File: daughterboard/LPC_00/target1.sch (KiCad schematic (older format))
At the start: 8 parts, among them U1 LPC1114FDH28_102_5

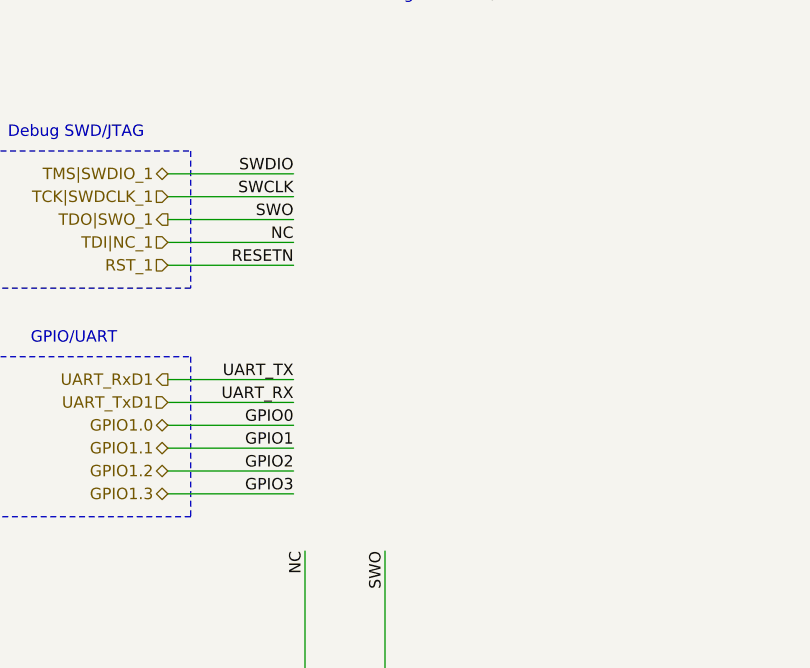
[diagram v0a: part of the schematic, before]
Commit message: added testpoints to daughterboards, updated readme
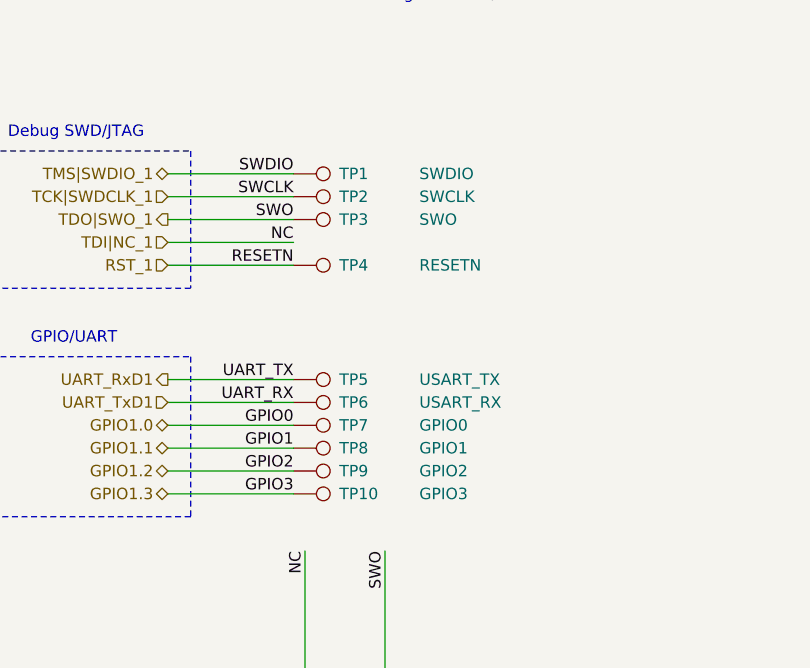
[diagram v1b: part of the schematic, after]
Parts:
- added TP1: SWDIO, symbol Connector:TestPoint
- added TP10: GPIO3, symbol Connector:TestPoint
- added TP2: SWCLK, symbol Connector:TestPoint
- added TP3: SWO, symbol Connector:TestPoint
- added TP4: RESETN, symbol Connector:TestPoint
- added TP5: USART_TX, symbol Connector:TestPoint
- added TP6: USART_RX, symbol Connector:TestPoint
- added TP7: GPIO0, symbol Connector:TestPoint
- added TP8: GPIO1, symbol Connector:TestPoint
- added TP9: GPIO2, symbol Connector:TestPoint
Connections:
- net GPIO1.0: now also TP7.1
- net GPIO1.1: now also TP8.1
- net GPIO1.2: now also TP9.1
- net GPIO1.3: now also TP10.1
- net RST_1: now also TP4.1
- net TCK|SWDCLK_1: now also TP2.1
- net TDO|SWO_1: now also TP3.1
- net TMS|SWDIO_1: now also TP1.1
- net UART_RxD1: now also TP5.1
- net UART_TxD1: now also TP6.1
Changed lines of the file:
@@
 NoConn ~ 5200 3650
 NoConn ~ 5200 3850
+$Comp
+L Connector:TestPoint TP?
+U 1 1 6191DBB6
+P 2150 1700
+AR Path="/616688D6/6191DBB6" Ref="TP?"  Part="1"
+AR Path="/61667F91/6191DBB6" Ref="TP1"  Part="1"
+F 0 "TP1" V 2150 1900 50  0000 L CNN
+F 1 "SWDIO" V 2150 2250 50  0000 L CNN
+F 2 "" H 2350 1700 50  0001 C CNN
+F 3 "~" H 2350 1700 50  0001 C CNN
+	1    2150 1700
+	0    1    1    0
+$EndComp
+$Comp
+L Connector:TestPoint TP?
+U 1 1 6191DBBC
+P 2150 1800
+AR Path="/616688D6/6191DBBC" Ref="TP?"  Part="1"
+AR Path="/61667F91/6191DBBC" Ref="TP2"  Part="1"
+F 0 "TP2" V 2150 2000 50  0000 L CNN
+F 1 "SWCLK" V 2150 2350 50  0000 L CNN
+F 2 "" H 2350 1800 50  0001 C CNN
+F 3 "~" H 2350 1800 50  0001 C CNN
+	1    2150 1800
+	0    1    1    0
+$EndComp
+$Comp
+L Connector:TestPoint TP?
+U 1 1 6191DBC2
+P 2150 1900
+AR Path="/616688D6/6191DBC2" Ref="TP?"  Part="1"
+AR Path="/61667F91/6191DBC2" Ref="TP3"  Part="1"
+F 0 "TP3" V 2150 2100 50  0000 L CNN
+F 1 "SWO" V 2150 2450 50  0000 L CNN
+F 2 "" H 2350 1900 50  0001 C CNN
+F 3 "~" H 2350 1900 50  0001 C CNN
+	1    2150 1900
+	0    1    1    0
+$EndComp
+$Comp
+L Connector:TestPoint TP?
+U 1 1 6191DBC8
+P 2150 2100
+AR Path="/616688D6/6191DBC8" Ref="TP?"  Part="1"
+AR Path="/61667F91/6191DBC8" Ref="TP4"  Part="1"
+F 0 "TP4" V 2150 2300 50  0000 L CNN
+F 1 "RESETN" V 2150 2650 50  0000 L CNN
+F 2 "" H 2350 2100 50  0001 C CNN
+F 3 "~" H 2350 2100 50  0001 C CNN
+	1    2150 2100
+	0    1    1    0
+$EndComp
+$Comp
+L Connector:TestPoint TP?
+U 1 1 6191DBCE
+P 2150 2600
+AR Path="/616688D6/6191DBCE" Ref="TP?"  Part="1"
+AR Path="/61667F91/6191DBCE" Ref="TP5"  Part="1"
+F 0 "TP5" V 2150 2800 50  0000 L CNN
+F 1 "USART_TX" V 2150 3150 50  0000 L CNN
+F 2 "" H 2350 2600 50  0001 C CNN
+F 3 "~" H 2350 2600 50  0001 C CNN
+	1    2150 2600
+	0    1    1    0
+$EndComp
+$Comp
+L Connector:TestPoint TP?
+U 1 1 6191DBD4
+P 2150 2700
+AR Path="/616688D6/6191DBD4" Ref="TP?"  Part="1"
+AR Path="/61667F91/6191DBD4" Ref="TP6"  Part="1"
+F 0 "TP6" V 2150 2900 50  0000 L CNN
+F 1 "USART_RX" V 2150 3250 50  0000 L CNN
+F 2 "" H 2350 2700 50  0001 C CNN
+F 3 "~" H 2350 2700 50  0001 C CNN
+	1    2150 2700
+	0    1    1    0
+$EndComp
+$Comp
+L Connector:TestPoint TP?
+U 1 1 6191DBDA
+P 2150 2800
+AR Path="/616688D6/6191DBDA" Ref="TP?"  Part="1"
+AR Path="/61667F91/6191DBDA" Ref="TP7"  Part="1"
+F 0 "TP7" V 2150 3000 50  0000 L CNN
+F 1 "GPIO0" V 2150 3350 50  0000 L CNN
+F 2 "" H 2350 2800 50  0001 C CNN
+F 3 "~" H 2350 2800 50  0001 C CNN
+	1    2150 2800
+	0    1    1    0
+$EndComp
+$Comp
+L Connector:TestPoint TP?
+U 1 1 6191DBE0
+P 2150 2900
+AR Path="/616688D6/6191DBE0" Ref="TP?"  Part="1"
+AR Path="/61667F91/6191DBE0" Ref="TP8"  Part="1"
+F 0 "TP8" V 2150 3100 50  0000 L CNN
+F 1 "GPIO1" V 2150 3450 50  0000 L CNN
+F 2 "" H 2350 2900 50  0001 C CNN
+F 3 "~" H 2350 2900 50  0001 C CNN
+	1    2150 2900
+	0    1    1    0
+$EndComp
+$Comp
+L Connector:TestPoint TP?
+U 1 1 6191DBE6
+P 2150 3000
+AR Path="/616688D6/6191DBE6" Ref="TP?"  Part="1"
+AR Path="/61667F91/6191DBE6" Ref="TP9"  Part="1"
+F 0 "TP9" V 2150 3200 50  0000 L CNN
+F 1 "GPIO2" V 2150 3550 50  0000 L CNN
+F 2 "" H 2350 3000 50  0001 C CNN
+F 3 "~" H 2350 3000 50  0001 C CNN
+	1    2150 3000
+	0    1    1    0
+$EndComp
+$Comp
+L Connector:TestPoint TP?
+U 1 1 6191DBEC
+P 2150 3100
+AR Path="/616688D6/6191DBEC" Ref="TP?"  Part="1"
+AR Path="/61667F91/6191DBEC" Ref="TP10"  Part="1"
+F 0 "TP10" V 2150 3300 50  0000 L CNN
+F 1 "GPIO3" V 2150 3650 50  0000 L CNN
+F 2 "" H 2350 3100 50  0001 C CNN
+F 3 "~" H 2350 3100 50  0001 C CNN
+	1    2150 3100
+	0    1    1    0
+$EndComp
 $EndSCHEMATC

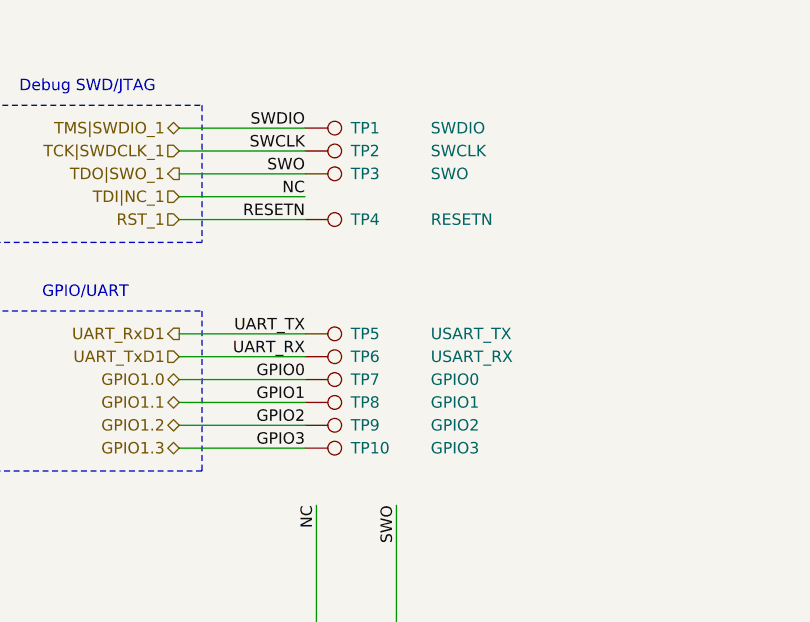
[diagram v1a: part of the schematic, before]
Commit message: sarted with LPC daughterboard layout
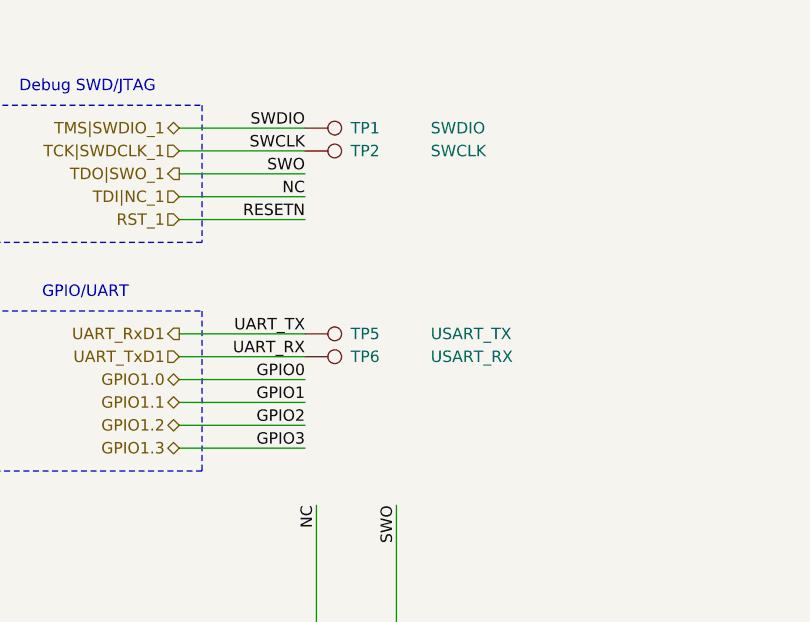
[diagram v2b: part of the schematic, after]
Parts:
- removed TP10: GPIO3, symbol Connector:TestPoint
- removed TP3: SWO, symbol Connector:TestPoint
- removed TP4: RESETN, symbol Connector:TestPoint
- removed TP7: GPIO0, symbol Connector:TestPoint
- removed TP8: GPIO1, symbol Connector:TestPoint
- removed TP9: GPIO2, symbol Connector:TestPoint
- C1, C2, C3: footprint (none) -> Capacitor_SMD:C_0603_1608Metric_Pad1.05x0.95mm_HandSolder
- JP1: footprint (none) -> Jumper:SolderJumper-2_P1.3mm_Open_TrianglePad1.0x1.5mm
- R1, R2, R3: footprint (none) -> Resistor_SMD:R_0603_1608Metric_Pad1.05x0.95mm_HandSolder
- TP1, TP2, TP5, TP6: footprint (none) -> TestPoint:TestPoint_Pad_1.0x1.0mm
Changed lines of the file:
@@
 F 0 "R2" H 2259 4346 50  0000 L CNN
 F 1 "100k" H 2259 4255 50  0000 L CNN
-F 2 "" H 2200 4300 50  0001 C CNN
+F 2 "Resistor_SMD:R_0603_1608Metric_Pad1.05x0.95mm_HandSolder" H 2200 4300 50  0001 C CNN
 F 3 "~" H 2200 4300 50  0001 C CNN
 	1    2200 4300
@@
 F 0 "R1" H 859 4346 50  0000 L CNN
 F 1 "100k" H 859 4255 50  0000 L CNN
-F 2 "" H 800 4300 50  0001 C CNN
+F 2 "Resistor_SMD:R_0603_1608Metric_Pad1.05x0.95mm_HandSolder" H 800 4300 50  0001 C CNN
 F 3 "~" H 800 4300 50  0001 C CNN
 	1    800  4300
@@
 F 0 "JP1" V 1404 4368 50  0000 L CNN
 F 1 "NRST" V 1495 4368 50  0000 L CNN
-F 2 "" H 1450 4300 50  0001 C CNN
+F 2 "Jumper:SolderJumper-2_P1.3mm_Open_TrianglePad1.0x1.5mm" H 1450 4300 50  0001 C CNN
 F 3 "~" H 1450 4300 50  0001 C CNN
 	1    1450 4300
@@
 F 0 "R3" H 2609 4346 50  0000 L CNN
 F 1 "100k" H 2609 4255 50  0000 L CNN
-F 2 "" H 2550 4300 50  0001 C CNN
+F 2 "Resistor_SMD:R_0603_1608Metric_Pad1.05x0.95mm_HandSolder" H 2550 4300 50  0001 C CNN
 F 3 "~" H 2550 4300 50  0001 C CNN
 	1    2550 4300
@@
 F 0 "C2" H 7892 2046 50  0000 L CNN
 F 1 "100n" H 7892 1955 50  0000 L CNN
-F 2 "" H 7800 2000 50  0001 C CNN
+F 2 "Capacitor_SMD:C_0603_1608Metric_Pad1.05x0.95mm_HandSolder" H 7800 2000 50  0001 C CNN
 F 3 "~" H 7800 2000 50  0001 C CNN
 	1    7800 2000
@@
 F 0 "C3" H 8292 2046 50  0000 L CNN
 F 1 "100n" H 8292 1955 50  0000 L CNN
-F 2 "" H 8200 2000 50  0001 C CNN
+F 2 "Capacitor_SMD:C_0603_1608Metric_Pad1.05x0.95mm_HandSolder" H 8200 2000 50  0001 C CNN
 F 3 "~" H 8200 2000 50  0001 C CNN
 	1    8200 2000
@@
 F 0 "C1" H 7392 2046 50  0000 L CNN
 F 1 "4.7u" H 7392 1955 50  0000 L CNN
-F 2 "" H 7300 2000 50  0001 C CNN
+F 2 "Capacitor_SMD:C_0603_1608Metric_Pad1.05x0.95mm_HandSolder" H 7300 2000 50  0001 C CNN
 F 3 "~" H 7300 2000 50  0001 C CNN
 	1    7300 2000
@@
 F 0 "TP1" V 2150 1900 50  0000 L CNN
 F 1 "SWDIO" V 2150 2250 50  0000 L CNN
-F 2 "" H 2350 1700 50  0001 C CNN
+F 2 "TestPoint:TestPoint_Pad_1.0x1.0mm" H 2350 1700 50  0001 C CNN
 F 3 "~" H 2350 1700 50  0001 C CNN
 	1    2150 1700
@@
 F 0 "TP2" V 2150 2000 50  0000 L CNN
 F 1 "SWCLK" V 2150 2350 50  0000 L CNN
-F 2 "" H 2350 1800 50  0001 C CNN
+F 2 "TestPoint:TestPoint_Pad_1.0x1.0mm" H 2350 1800 50  0001 C CNN
 F 3 "~" H 2350 1800 50  0001 C CNN
 	1    2150 1800
-	0    1    1    0
-$EndComp
-$Comp
-L Connector:TestPoint TP?
-U 1 1 6191DBC2
-P 2150 1900
-AR Path="/616688D6/6191DBC2" Ref="TP?"  Part="1"
-AR Path="/61667F91/6191DBC2" Ref="TP3"  Part="1"
-F 0 "TP3" V 2150 2100 50  0000 L CNN
-F 1 "SWO" V 2150 2450 50  0000 L CNN
-F 2 "" H 2350 1900 50  0001 C CNN
-F 3 "~" H 2350 1900 50  0001 C CNN
-	1    2150 1900
-	0    1    1    0
-$EndComp
-$Comp
-L Connector:TestPoint TP?
-U 1 1 6191DBC8
-P 2150 2100
-AR Path="/616688D6/6191DBC8" Ref="TP?"  Part="1"
-AR Path="/61667F91/6191DBC8" Ref="TP4"  Part="1"
-F 0 "TP4" V 2150 2300 50  0000 L CNN
-F 1 "RESETN" V 2150 2650 50  0000 L CNN
-F 2 "" H 2350 2100 50  0001 C CNN
-F 3 "~" H 2350 2100 50  0001 C CNN
-	1    2150 2100
 	0    1    1    0
 $EndComp
@@
 F 0 "TP5" V 2150 2800 50  0000 L CNN
 F 1 "USART_TX" V 2150 3150 50  0000 L CNN
-F 2 "" H 2350 2600 50  0001 C CNN
+F 2 "TestPoint:TestPoint_Pad_1.0x1.0mm" H 2350 2600 50  0001 C CNN
 F 3 "~" H 2350 2600 50  0001 C CNN
 	1    2150 2600
@@
 F 0 "TP6" V 2150 2900 50  0000 L CNN
 F 1 "USART_RX" V 2150 3250 50  0000 L CNN
-F 2 "" H 2350 2700 50  0001 C CNN
+F 2 "TestPoint:TestPoint_Pad_1.0x1.0mm" H 2350 2700 50  0001 C CNN
 F 3 "~" H 2350 2700 50  0001 C CNN
 	1    2150 2700
 	0    1    1    0
 $EndComp
-$Comp
-L Connector:TestPoint TP?
-U 1 1 6191DBDA
-P 2150 2800
-AR Path="/616688D6/6191DBDA" Ref="TP?"  Part="1"
-AR Path="/61667F91/6191DBDA" Ref="TP7"  Part="1"
-F 0 "TP7" V 2150 3000 50  0000 L CNN
-F 1 "GPIO0" V 2150 3350 50  0000 L CNN
-F 2 "" H 2350 2800 50  0001 C CNN
-F 3 "~" H 2350 2800 50  0001 C CNN
-	1    2150 2800
-	0    1    1    0
-$EndComp
-$Comp
-L Connector:TestPoint TP?
-U 1 1 6191DBE0
-P 2150 2900
-AR Path="/616688D6/6191DBE0" Ref="TP?"  Part="1"
-AR Path="/61667F91/6191DBE0" Ref="TP8"  Part="1"
-F 0 "TP8" V 2150 3100 50  0000 L CNN
-F 1 "GPIO1" V 2150 3450 50  0000 L CNN
-F 2 "" H 2350 2900 50  0001 C CNN
-F 3 "~" H 2350 2900 50  0001 C CNN
-	1    2150 2900
-	0    1    1    0
-$EndComp
-$Comp
-L Connector:TestPoint TP?
-U 1 1 6191DBE6
-P 2150 3000
-AR Path="/616688D6/6191DBE6" Ref="TP?"  Part="1"
-AR Path="/61667F91/6191DBE6" Ref="TP9"  Part="1"
-F 0 "TP9" V 2150 3200 50  0000 L CNN
-F 1 "GPIO2" V 2150 3550 50  0000 L CNN
-F 2 "" H 2350 3000 50  0001 C CNN
-F 3 "~" H 2350 3000 50  0001 C CNN
-	1    2150 3000
-	0    1    1    0
-$EndComp
-$Comp
-L Connector:TestPoint TP?
-U 1 1 6191DBEC
-P 2150 3100
-AR Path="/616688D6/6191DBEC" Ref="TP?"  Part="1"
-AR Path="/61667F91/6191DBEC" Ref="TP10"  Part="1"
-F 0 "TP10" V 2150 3300 50  0000 L CNN
-F 1 "GPIO3" V 2150 3650 50  0000 L CNN
-F 2 "" H 2350 3100 50  0001 C CNN
-F 3 "~" H 2350 3100 50  0001 C CNN
-	1    2150 3100
-	0    1    1    0
-$EndComp

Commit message: further work on LPC layout
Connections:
- net +3V3: now also C1.1, C2.1, C3.1, U1.21 (VDD), U1.7 (VDDA)
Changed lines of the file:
@@
 	0    1    1    0
 $EndComp
+$Comp
+L power:+3V3 #PWR?
+U 1 1 61934697
+P 8200 1700
+F 0 "#PWR?" H 8200 1550 50  0001 C CNN
+F 1 "+3V3" H 8215 1873 50  0000 C CNN
+F 2 "" H 8200 1700 50  0001 C CNN
+F 3 "" H 8200 1700 50  0001 C CNN
+	1    8200 1700
+	1    0    0    -1
+$EndComp
+Wire Wire Line
+	8200 1700 8200 1800
+Connection ~ 8200 1800
 $EndSCHEMATC
